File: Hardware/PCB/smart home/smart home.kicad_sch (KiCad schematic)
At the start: 52 parts, among them M1 Fan, Q1 BC547, Q10 BC547C, Q2 BC547C, Q3 BC547C, Q4 BC547C, Q5 BC547C, Q6 BC547C, Q7 BC547C, Q8 BC547C, Q9 BC547C, SW1 SW_SPST, SW2 SW_SPST, SW3 SW_SPST, SW4 SW_Push, SW5 SW_Push, SW6 SW_Push

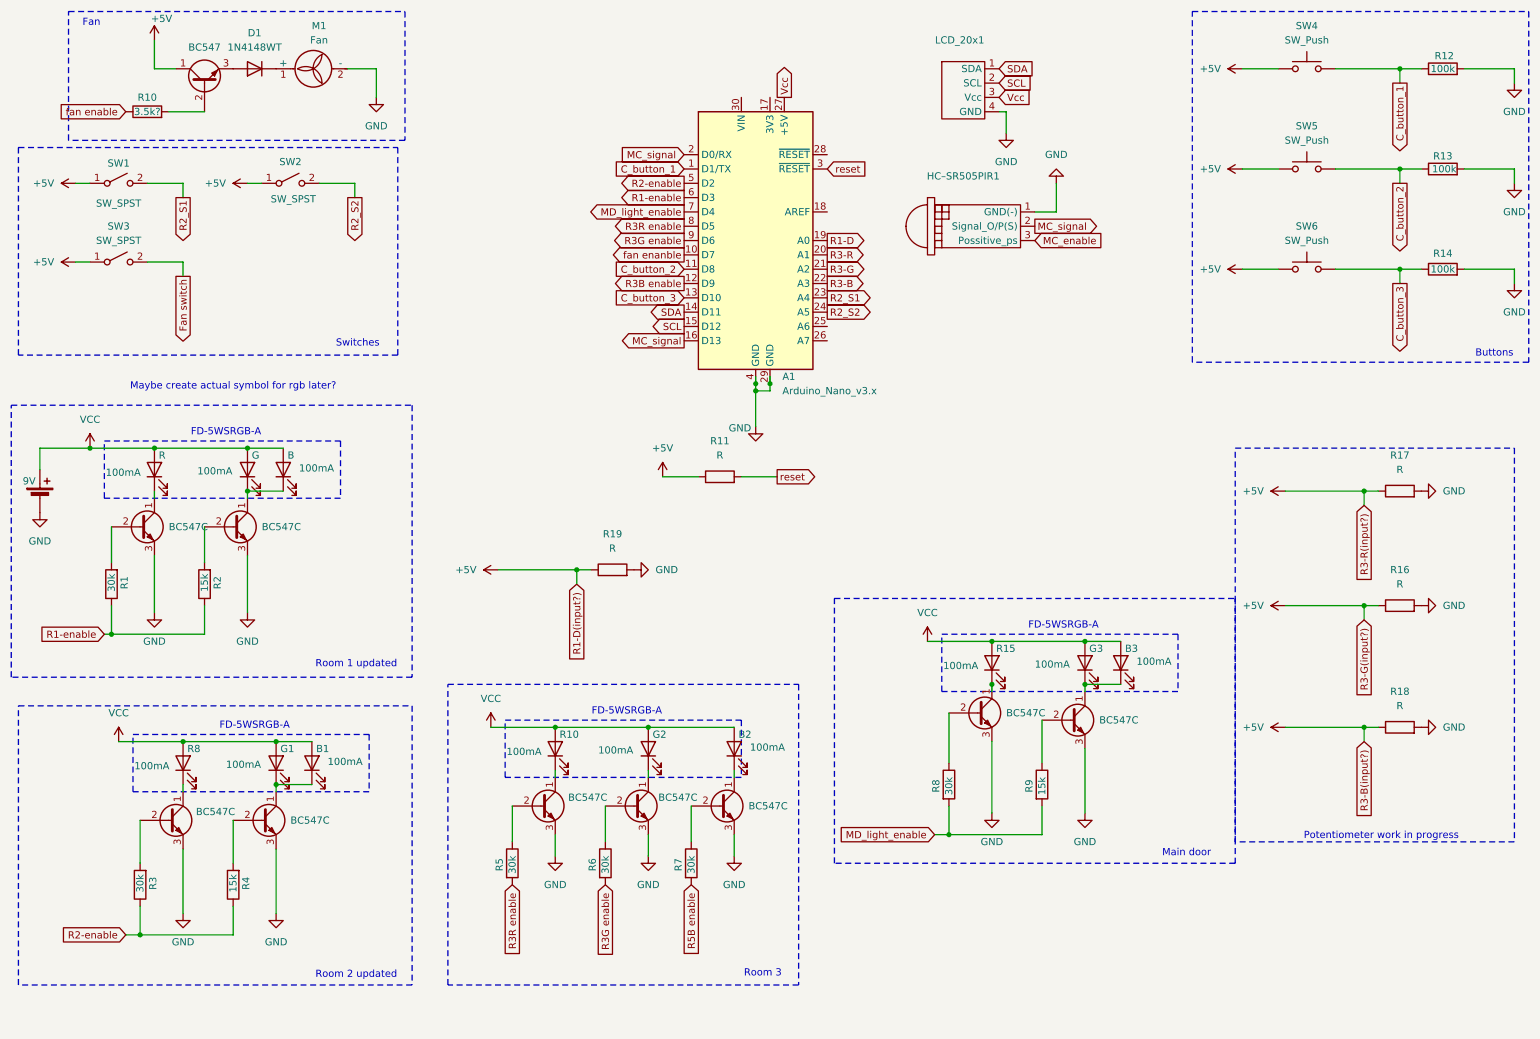
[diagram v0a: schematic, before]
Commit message: cleaning up elec scheme + pot + rgb custom models
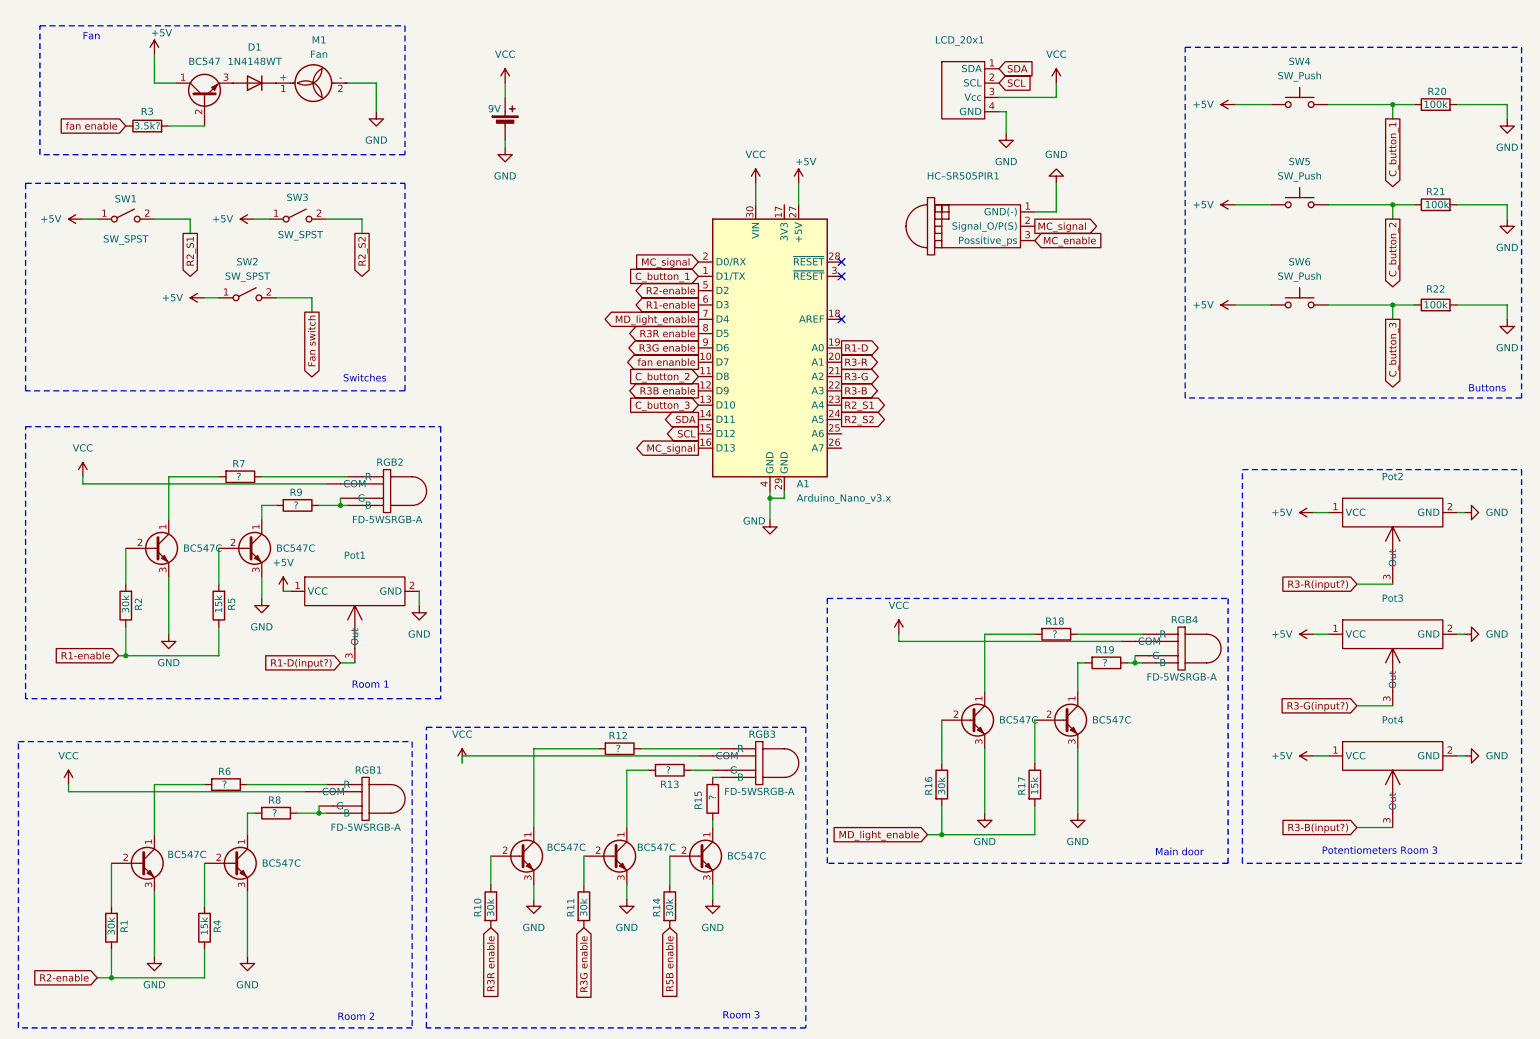
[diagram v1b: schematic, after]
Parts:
- removed B, G, R: 100mA, https://www.snapeda.com/parts/HC-SR505/TruSens/datasheet/, symbol Device:LED
- removed B1, B2, B3, G1, G2, G3, R10, R15, R8: 100mA, symbol Device:LED
- removed R11, R16, R17: R, symbol Device:R
- added Pot1, Pot2, Pot3, Pot4: ~, symbol smarthome:Pot
- added R12, R13, R15, R6, R7, R8, R9: ?, symbol Device:R
- added RGB1, RGB2, RGB3, RGB4: FD-5WSRGB-A, symbol smarthome:RGB
- R18, R19: value R -> ?
- renumbered Q4 to Q1, Q3 to Q2, Q1 to Q3, Q5 to Q4, Q2 to Q5, R3 to R1, R5 to R10, R6 to R11, R7 to R14, R8 to R16, R9 to R17, R1 to R2, R12 to R20, R13 to R21, R14 to R22, R10 to R3, R2 to R5, SW3 to SW2, SW2 to SW3
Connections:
- net +5V: now also A1.27 (+5V), Pot1.1 (VCC), Pot2.1 (VCC), Pot3.1 (VCC), Pot4.1 (VCC); no longer R18.1, R19.1
- net GND: now also Pot1.2 (GND), Pot2.2 (GND), Pot3.2 (GND), Pot4.2 (GND); no longer R18.2, R19.2
- net VCC: now also A1.30 (VIN), LCD_20x1.3 (Vcc), RGB1. (R), RGB2. (R), RGB3. (R), RGB4. (R)
- net at Q7.1 (C): now also R13.2
- net at Q10.1 (C): now also R19.2
- net at Q1.1 (C): now also R6.2
- net at Q8.1 (C): now also R15.1
- net at Q2.1 (C): now also R7.2
- net at Q9.1 (C): now also R18.2
- net at Q5.1 (C): now also R9.2
- net at Q4.1 (C): now also R8.2
- net at Q6.1 (C): now also R12.2
- removed net Vcc: A1.27 (+5V), LCD_20x1.3 (Vcc)
- net reset: no longer names the net of A1.3 (~{RESET})
- new net: R19.1, RGB4. (R)
- new net: R18.1, RGB4. (R)
- new net: R12.1, RGB3. (R)
- new net: R9.1, RGB2. (R)
- new net: R7.1, RGB2. (R)
- new net: R15.2, RGB3. (R)
- new net: R13.1, RGB3. (R)
- new net: R6.1, RGB1. (R)
- new net: R8.1, RGB1. (R)
- new net R1-D(input?): Pot1.3 (Out)
- new net R3-B(input?): Pot4.3 (Out)
- new net R3-G(input?): Pot3.3 (Out)
- new net R3-R(input?): Pot2.3 (Out)
- no-connect marks 0 -> 3
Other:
- note added: "Potentiometers Room 3"
- note added: "Room 1"
- note added: "Room 2"
- note removed: "FD-5WSRGB-A"
- note removed: "Maybe create actual symbol for rgb later?"
- note removed: "Potentiometer work in progress"
- note removed: "Room 1 updated"
- note removed: "Room 2 updated"
- company: group 8 -> Group 4
- moved on the sheet: A1, D1, M1, R1, R10, R11, R14, R16, R17, R2, R20, R21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

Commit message: PCB should be right about done
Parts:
- removed Q10, Q4, Q5: BC547C, Package_TO_SOT_THT:TO-92_Inline, symbol Transistor_BJT:BC547
- removed R17: 15k, symbol Device:R
- added R23: LDR03, OptoDevice:R_LDR_10x8.5mm_P7.6mm_Vertical, symbol Sensor_Optical:LDR03
- added R24: 300, symbol Device:R
- added SW7: SW_SPST, symbol Switch:SW_SPST
- R10, R11, R14: value 30k -> 90k
- R12, R18, R7: value ? -> 360
- R13, R15, R19, R6, R8, R9: value ? -> 300
- R3: value 3.5k? -> 5k
- R4: value 15k -> 360
- R5: value 15k -> 300
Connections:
- net +5V: now also R23.1, SW7.1 (A)
- net C_button_3: now also A1.7 (D4); no longer A1.13 (D10)
- net MD_light_enable: now also A1.13 (D10); no longer A1.7 (D4)
- net R1-enable: no longer R5.1
- net R2-enable: no longer R4.1
- net R2_S1: now also A1.10 (D7); no longer A1.23 (A4)
- net R2_S2: now also A1.15 (D12); no longer A1.24 (A5)
- net SCL: now also A1.24 (A5); no longer A1.15 (D12)
- net SDA: now also A1.23 (A4); no longer A1.14 (D11)
- net fan enanble: now also A1.14 (D11); no longer A1.10 (D7)
- net at Q1.1 (C), R6.2: now also R4.2, R5.2
- net at Q2.1 (C), R7.2: now also R9.2, R24.2
- net at Q9.1 (C), R18.2: now also R19.2, R8.2
- net at R8.1: now also RGB4. (R); no longer RGB1. (R)
- net LDR: now reaches A1.25 (A6)
- net LDR: now also R23.2
- net R3_S1: now reaches A1.26 (A7)
- net R3_S1: now also SW7.2 (B)
- new net: R5.1, RGB1. (R)
- new net: R4.1, RGB1. (R)
- new net: R24.1, RGB2. (R)
- no-connect marks 3 -> 4
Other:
- moved on the sheet: R10, R11, R14, R3, SW2

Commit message: revision changed
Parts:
- R1, R16, R2: value 30k -> 15k
- R10, R11, R14: value 90k -> 45k
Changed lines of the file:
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@@
 		(title "Semester project (smart house)")
 		(date "2024-10-23")
-		(rev "G man vol.2")
+		(rev "v6")
 		(company "Group 4")
-		(comment 3 "R values must be calculated (correctly)")
-		(comment 4 "Needs some cleaning up")
 	)
 	(junction
@@
 			)
 		)
-		(property "Value" "30k"
+		(property "Value" "15k"
 			(at 179.07 150.114 90)
 			(effects
@@
 	)
 	(symbol
-		(lib_name "smarthome:RGB")
 		(lib_id "smarthome:RGB")
 		(at 80.01 153.67 270)
@@
 			)
 		)
-		(property "Value" "90k"
+		(property "Value" "45k"
 			(at 115.57 169.164 90)
 			(effects
@@
 			)
 		)
-		(property "Value" "30k"
+		(property "Value" "15k"
 			(at 34.29 117.856 90)
 			(effects
@@
 			)
 		)
-		(property "Value" "90k"
+		(property "Value" "45k"
 			(at 130.81 169.164 90)
 			(effects
@@
 	)
 	(symbol
-		(lib_name "smarthome:RGB")
 		(lib_id "smarthome:RGB")
 		(at 83.82 97.79 270)
@@
 			)
 		)
-		(property "Value" "90k"
+		(property "Value" "45k"
 			(at 99.06 169.164 90)
 			(effects
@@
 			)
 		)
-		(property "Value" "30k"
+		(property "Value" "15k"
 			(at 30.48 173.736 90)
 			(effects
